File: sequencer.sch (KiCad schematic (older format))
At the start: 189 parts, among them IC1 ATMEGA328PB, IC2 AT24CS64-XHM, J13 SYNC IN, J14 TRIGGER OUT 1, J15 TRIGGER OUT 2, P3 CONN_02X02, P4 CONN_02X03, P5 CONN_02X03, P6 CONN_01X03, P7 CONN_01X04, Q38 MMBT3904, SW10 INST_CH_12, SW11 SHIFT, SW12 IF_VAR, SW13 INST_LT_4, SW14 INST_MT_5, SW15 INST_HT_6, SW16 INST_RS_7, SW17 INST_CP_8, SW18 INST_CB_9, SW19 INST_CY_10, SW2 BASIC_VAR_A, SW20 INST_OH_11, SW21 START/STOP, SW22 TAP, SW4 MODE, SW5 FILL, SW6 CLEAR, SW7 INST_AC_1, SW8 INST_BD_2, SW9 INST_SD_3, U27 74HC165, U28 74HC165, U29 74HC165, U30 74AC595, U31 74AC595, U32 74AC595, U33 74AC595, U34 74AC595, U35 R-78E5.0-1.0, U36 74AC595, U37 74AC595, X1 MIDI IN, Y1 16MHz

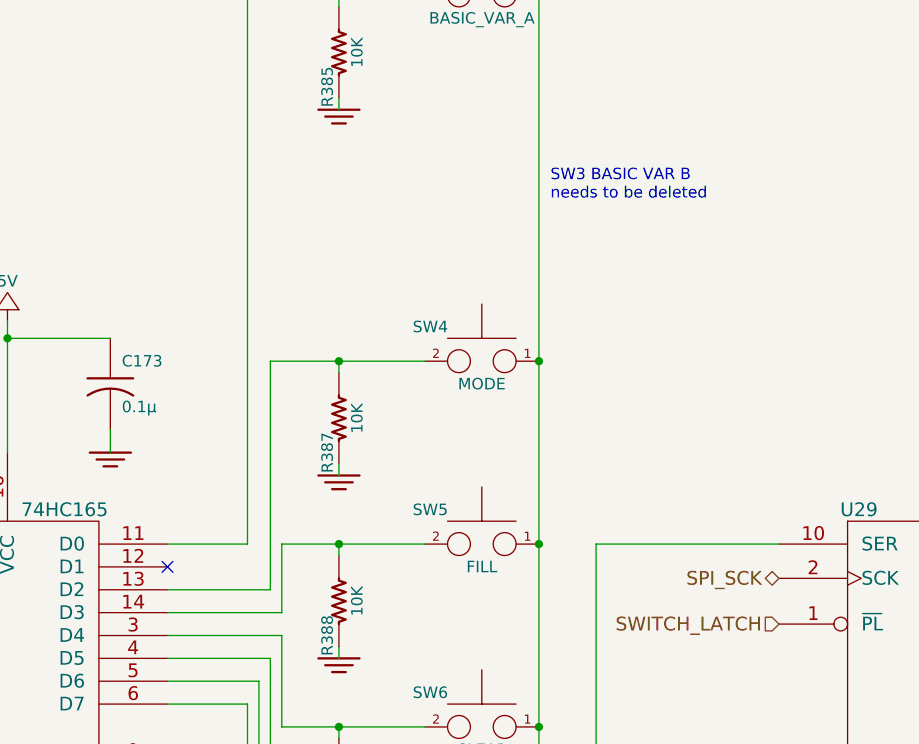
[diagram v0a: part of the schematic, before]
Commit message: made some notes on schematics. added beginnings of OM
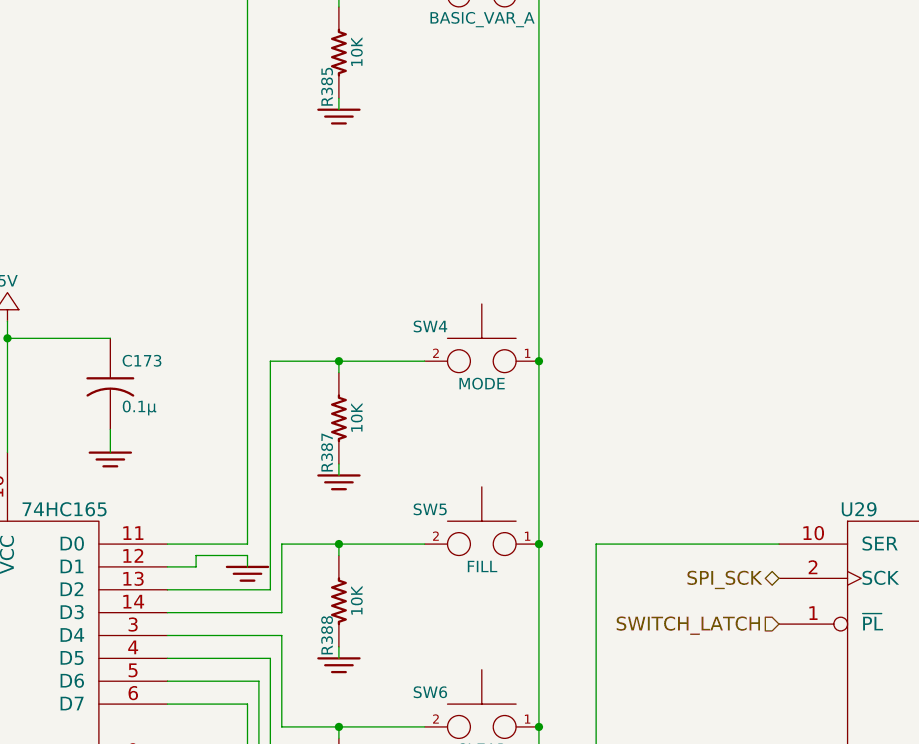
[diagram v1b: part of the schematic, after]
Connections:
- wire segments 592 -> 596
- no-connect marks 10 -> 9
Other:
- note removed: "SW3 BASIC VAR B \nneeds to be deleted"
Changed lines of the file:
@@
 Text GLabel 12700 3375 2    50   Input ~ 0
 SYNC_IN
-Text Notes 4325 6400 0    50   ~ 0
-SW3 BASIC VAR B \nneeds to be deleted
 Text GLabel 12700 2625 2    50   Output ~ 0
 SYNC_LED_R
@@
 Wire Wire Line
 	10675 10325 11100 10325
-NoConn ~ 2650 8000
 $Comp
 L GND_E #PWR0486
@@
 Wire Wire Line
 	7175 3825 7250 3825
+$Comp
+L GND_E #PWR?
+U 1 1 5893EC46
+P 3000 8000
+F 0 "#PWR?" V 3000 8000 30  0001 C CNN
+F 1 "GND_E" H 3000 7930 30  0001 C CNN
+F 2 "~" H 3000 8000 60  0000 C CNN
+F 3 "~" H 3000 8000 60  0000 C CNN
+	1    3000 8000
+	1    0    0    -1
+$EndComp
+Wire Wire Line
+	2650 8000 2775 8000
+Wire Wire Line
+	2775 8000 2775 7950
+Wire Wire Line
+	2775 7950 3000 7950
+Wire Wire Line
+	3000 7950 3000 8000
 $EndSCHEMATC

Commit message: added 47uF caps to 5V supplies for U37 and U37. required to reduce SPI noise
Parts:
- added C164, C166: 47μ, MyModules:jrl_c_elec_5x5.3, symbol CP_US
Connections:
- wire segments 596 -> 600
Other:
- note added: "BIG FAT DIGITAL RAIL\nFILTER CAP"
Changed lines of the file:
@@
 	7175 3825 7250 3825
 $Comp
-L GND_E #PWR?
+L GND_E #PWR0489
 U 1 1 5893EC46
 P 3000 8000
-F 0 "#PWR?" V 3000 8000 30  0001 C CNN
+F 0 "#PWR0489" V 3000 8000 30  0001 C CNN
 F 1 "GND_E" H 3000 7930 30  0001 C CNN
 F 2 "~" H 3000 8000 60  0000 C CNN
@@
 Wire Wire Line
 	3000 7950 3000 8000
+$Comp
+L CP_US C164
+U 1 1 58D6CD8E
+P 18050 6550
+F 0 "C164" H 18075 6650 50  0000 L CNN
+F 1 "47μ" H 18075 6425 50  0000 L CNN
+F 2 "MyModules:jrl_c_elec_5x5.3" H 18050 6550 60  0001 C CNN
+F 3 "" H 18050 6550 60  0000 C CNN
+	1    18050 6550
+	1    0    0    -1
+$EndComp
+$Comp
+L CP_US C166
+U 1 1 58D6CD95
+P 18050 10200
+F 0 "C166" H 18075 10300 50  0000 L CNN
+F 1 "47μ" H 18075 10075 50  0000 L CNN
+F 2 "MyModules:jrl_c_elec_5x5.3" H 18050 10200 60  0001 C CNN
+F 3 "" H 18050 10200 60  0000 C CNN
+	1    18050 10200
+	1    0    0    -1
+$EndComp
+Connection ~ 18050 10000
+Wire Wire Line
+	18050 10400 18050 10450
+Wire Wire Line
+	18050 10450 18300 10450
+Connection ~ 18300 10450
+Text Notes 18125 9950 1    60   ~ 0
+BIG FAT DIGITAL RAIL\nFILTER CAP
+Connection ~ 18050 6350
+Wire Wire Line
+	18050 6750 18050 6800
+Wire Wire Line
+	18050 6800 18300 6800
+Connection ~ 18300 6800
+Text Notes 18250 6300 1    60   ~ 0
+BIG FAT DIGITAL RAIL\nFILTER CAP
 $EndSCHEMATC

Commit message: all triggers consolidated into one connector
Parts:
- removed P3: CONN_02X02, MyModules:GH-TOP-4, symbol CONN_02X02
- removed P4, P5: CONN_02X03, MyModules:GH-TOP-6, symbol CONN_02X03
- added P3: CONN_02X10, Pin_Headers:Pin_Header_Straight_2x10_Pitch1.27mm_SMD, symbol CONN_02X10
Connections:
- net labels added: COMMON_TRIG
- wire segments 600 -> 604
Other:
- note added: "TRIGGER \nHEADER"
- note removed: "TRIGGER \nHEADERS"
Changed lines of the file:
@@
 	17850 6275 17850 6850
 Wire Wire Line
-	18300 6350 17850 6350
+	17850 6350 18300 6350
 Wire Wire Line
 	17850 8550 17850 8650
@@
 	17850 9950 17850 10500
 Wire Wire Line
-	18300 10000 17850 10000
+	17850 10000 18300 10000
 Wire Wire Line
 	17850 12200 17850 12300
@@
 Wire Wire Line
 	4600 3975 4750 3975
-$Comp
-L CONN_02X02 P3
-U 1 1 57DD315C
-P 11125 9325
-F 0 "P3" H 11125 9525 50  0000 C CNN
-F 1 "CONN_02X02" H 11125 9175 50  0000 C CNN
-F 2 "MyModules:GH-TOP-4" H 11125 8125 60  0001 C CNN
-F 3 "" H 11125 8125 60  0000 C CNN
-	1    11125 9325
-	1    0    0    -1
-$EndComp
-Text HLabel 9450 9225 0    50   Output ~ 0
+Text HLabel 11100 9000 0    50   Output ~ 0
 ACCENT
-Text HLabel 9950 9225 2    50   Output ~ 0
+Text HLabel 11100 9100 0    50   Output ~ 0
 BD_TRIG
-Text HLabel 9450 9325 0    50   Output ~ 0
+Text HLabel 11100 9300 0    50   Output ~ 0
 SD_TRIG
-Text HLabel 9950 9325 2    50   Output ~ 0
+Text HLabel 11100 9800 0    50   Output ~ 0
 LT_TRIG
-Text HLabel 9450 9425 0    50   Output ~ 0
+Text HLabel 11100 9700 0    50   Output ~ 0
 MT_TRIG
-Text HLabel 9950 9425 2    50   Output ~ 0
+Text HLabel 11100 9600 0    50   Output ~ 0
 HT_TRIG
-Text HLabel 10875 9275 0    50   Output ~ 0
+Text HLabel 11100 9500 0    50   Output ~ 0
 RS_TRIG
-Text HLabel 11375 9275 2    50   Output ~ 0
+Text HLabel 11100 9400 0    50   Output ~ 0
 CP_TRIG
 Text Notes 10950 8825 0    60   ~ 0
-TRIGGER \nHEADERS
+TRIGGER \nHEADER
 $Comp
 L GND_E #PWR0483
 U 1 1 57DD8A3A
-P 11475 9525
-F 0 "#PWR0483" V 11475 9525 30  0001 C CNN
-F 1 "GND_E" H 11475 9455 30  0001 C CNN
-F 2 "~" H 11475 9525 60  0000 C CNN
-F 3 "~" H 11475 9525 60  0000 C CNN
-	1    11475 9525
-	1    0    0    -1
-$EndComp
-Wire Wire Line
-	11375 9375 11475 9375
-Wire Wire Line
-	11475 9375 11475 9525
+P 12100 9550
+F 0 "#PWR0483" V 12100 9550 30  0001 C CNN
+F 1 "GND_E" H 12100 9480 30  0001 C CNN
+F 2 "~" H 12100 9550 60  0000 C CNN
+F 3 "~" H 12100 9550 60  0000 C CNN
+	1    12100 9550
+	1    0    0    -1
+$EndComp
 $Comp
 L 5V #PWR0484
 U 1 1 57DDA864
-P 10675 10050
-F 0 "#PWR0484" H 10675 9900 50  0001 C CNN
-F 1 "5V" H 10675 10225 50  0000 C CNN
-F 2 "" H 10675 10050 60  0000 C CNN
-F 3 "" H 10675 10050 60  0000 C CNN
-	1    10675 10050
-	1    0    0    -1
-$EndComp
-$Comp
-L CONN_02X03 P4
-U 1 1 57DDE11C
-P 11350 10225
-F 0 "P4" H 11350 10425 50  0000 C CNN
-F 1 "CONN_02X03" H 11350 10025 50  0000 C CNN
-F 2 "MyModules:GH-TOP-6" H 11350 9025 60  0001 C CNN
-F 3 "" H 11350 9025 60  0000 C CNN
-	1    11350 10225
-	1    0    0    -1
-$EndComp
-Text HLabel 10875 9375 0    50   Output ~ 0
+P 10300 8900
+F 0 "#PWR0484" H 10300 8750 50  0001 C CNN
+F 1 "5V" H 10300 9075 50  0000 C CNN
+F 2 "" H 10300 8900 60  0000 C CNN
+F 3 "" H 10300 8900 60  0000 C CNN
+	1    10300 8900
+	1    0    0    -1
+$EndComp
+Text HLabel 11100 9900 0    50   Output ~ 0
 MA_TRIG
-Text HLabel 11100 10125 0    50   Output ~ 0
+Text HLabel 11600 9700 2    50   Output ~ 0
 CB_TRIG
-Text HLabel 11600 10125 2    50   Output ~ 0
+Text HLabel 11600 9800 2    50   Output ~ 0
 CY_TRIG
-Text HLabel 11100 10225 0    50   Output ~ 0
+Text HLabel 11600 9900 2    50   Output ~ 0
 OH_TRIG
-Text HLabel 11600 10225 2    50   Output ~ 0
+Text HLabel 11600 9600 2    50   Output ~ 0
 CH_TRIG
 $Comp
 L GND_E #PWR0485
 U 1 1 57DE40B4
-P 11675 10500
-F 0 "#PWR0485" V 11675 10500 30  0001 C CNN
-F 1 "GND_E" H 11675 10430 30  0001 C CNN
-F 2 "~" H 11675 10500 60  0000 C CNN
-F 3 "~" H 11675 10500 60  0000 C CNN
-	1    11675 10500
-	1    0    0    -1
-$EndComp
-Wire Wire Line
-	11600 10325 11675 10325
-Wire Wire Line
-	11675 10325 11675 10500
-$Comp
-L CONN_02X03 P5
-U 1 1 57B54F0F
-P 9700 9325
-F 0 "P5" H 9700 9525 50  0000 C CNN
-F 1 "CONN_02X03" H 9700 9125 50  0000 C CNN
-F 2 "MyModules:GH-TOP-6" H 9700 8125 60  0001 C CNN
-F 3 "" H 9700 8125 60  0000 C CNN
-	1    9700 9325
-	1    0    0    -1
-$EndComp
-Wire Wire Line
-	10675 10050 10675 10325
-Wire Wire Line
-	10675 10325 11100 10325
+P 12450 7500
+F 0 "#PWR0485" V 12450 7500 30  0001 C CNN
+F 1 "GND_E" H 12450 7430 30  0001 C CNN
+F 2 "~" H 12450 7500 60  0000 C CNN
+F 3 "~" H 12450 7500 60  0000 C CNN
+	1    12450 7500
+	1    0    0    -1
+$EndComp
 $Comp
 L GND_E #PWR0486
@@
 Text Notes 18250 6300 1    60   ~ 0
 BIG FAT DIGITAL RAIL\nFILTER CAP
+$Comp
+L CONN_02X10 P3
+U 1 1 58DC7F14
+P 11350 9450
+F 0 "P3" H 11350 10000 50  0000 C CNN
+F 1 "CONN_02X10" V 11350 9450 50  0000 C CNN
+F 2 "Pin_Headers:Pin_Header_Straight_2x10_Pitch1.27mm_SMD" H 11350 8250 60  0000 C CNN
+F 3 "" H 11350 8250 60  0000 C CNN
+	1    11350 9450
+	1    0    0    -1
+$EndComp
+Text GLabel 11100 9200 0    60   Output ~ 0
+COMMON_TRIG
+$Comp
+L 5V #PWR0490
+U 1 1 58DF48F9
+P 11800 8900
+F 0 "#PWR0490" H 11800 8750 50  0001 C CNN
+F 1 "5V" H 11800 9075 50  0000 C CNN
+F 2 "" H 11800 8900 60  0000 C CNN
+F 3 "" H 11800 8900 60  0000 C CNN
+	1    11800 8900
+	1    0    0    -1
+$EndComp
+Wire Wire Line
+	10300 8900 10300 9000
+Wire Wire Line
+	10300 9000 10525 9000
+Wire Wire Line
+	11800 8900 11800 9100
+Wire Wire Line
+	11800 9000 11600 9000
+Wire Wire Line
+	11800 9100 11600 9100
+Connection ~ 11800 9000
+Wire Wire Line
+	11600 9200 12100 9200
+Wire Wire Line
+	12100 9200 12100 9550
+Wire Wire Line
+	11600 9300 12100 9300
+Connection ~ 12100 9300
+Wire Wire Line
+	11600 9400 12100 9400
+Connection ~ 12100 9400
+Wire Wire Line
+	11600 9500 12100 9500
+Connection ~ 12100 9500
 $EndSCHEMATC

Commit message: added 5V to 12V selectable trigger output for TRIG OUT 2
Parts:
- removed P7: CONN_01X04, MyModules:GH-TOP-4, symbol CONN_01X04
- removed Q38: MMBT3904, MyModules:SOT23-132-JRL, symbol MMBT3904
- added P12: CONN_01X03, Pin_Headers:Pin_Header_Straight_1x03_Pitch2.54mm, symbol CONN_01X03
- added P7: CONN_02X03, DIY:PIN_ARRAY_3X2, symbol CONN_02X03
- added Q38, Q64: C945, MyModules:SOT23-132-JRL, symbol C945
- added Q75: A733, MyModules:SOT23-132-JRL, symbol A733
- added R393, R457: 22K, MyModules:SM0603-R-JRL, symbol R_US
- added R456, R458: 10K, MyModules:SM0603-R-JRL, symbol R_US
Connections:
- net DIN_FILL: now also P7.2 (P2)
- net DIN_RESET: now also P7.1 (P1)
- net DIN_RUN_STOP: now also P7.4 (P4)
- net DIN_TEMPO_CLK: now also P7.6 (P6)
- net GND: now also P7.3 (P3), Q38.2 (E), Q64.2 (E), R456.1
- net SYNC_IN: now also Q38.3 (C)
- net TRIG_OUT_2: now also P12.3 (P3), R393.2; no longer J15.3
- net UART_TX: now also P7.5 (P5)
- net V+: now also Q75.3 (C), R458.2
- net at R380.2, R451.1: now also Q38.1 (B)
- new net: J15.3, P12.2 (P2)
- new net: Q64.1 (B), R393.1, R456.2
- new net: Q64.3 (C), R457.2
- new net: Q75.1 (B), R457.1, R458.1
- new net TRIG_OUT_12V: P12.1 (P1), Q75.2 (E)

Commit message: few tweaks, ready to generate gerbers for 2.1 production prototype
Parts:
- added P13, P14: CONN_01X01, MyModules:TEST_POINT_SMALL, symbol CONN_01X01
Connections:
- net +5V: now also P13.1 (P1)
- net GND: now also P14.1 (P1)

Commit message: added input protection fuses, fixed trigger level converter, few tweaks
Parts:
- added R459: 10K, MyModules:SM0603-R-JRL, symbol R_US
- R457: value 22K -> 10K
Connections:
- net GND: now also R459.1
- net TRIG_OUT_12V: now also Q75.3 (C), R459.2; no longer Q75.2 (E)
- net V+: now also Q75.2 (E); no longer Q75.3 (C)
- net at Q64.3 (C), R457.2: now also R458.1
- net at Q75.1 (B), R457.1: no longer R458.1
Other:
- note added: "CAT24C512\n"
- note added: "Need to add protection/\nrectification here?\n"
- moved on the sheet: R458
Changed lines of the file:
@@
 F 3 "" H 15200 4525 50  0000 L CNN
 	1    15200 4525
-	1    0    0    -1
+	1    0    0    1
 $EndComp
 Wire Wire Line
@@
 	14425 5025 14425 5350
 Wire Wire Line
-	14425 5350 14050 5350
+	14050 5350 15300 5350
 Wire Wire Line
 	14050 5300 14050 5425
@@
 L R_US R458
 U 1 1 5903EC77
-P 14975 4250
-F 0 "R458" H 15125 4200 50  0000 C CNN
-F 1 "10K" H 15100 4275 50  0000 C CNN
-F 2 "MyModules:SM0603-R-JRL" H 14975 4250 60  0001 C CNN
-F 3 "~" H 14975 4250 60  0000 C CNN
-	1    14975 4250
+P 14525 4250
+F 0 "R458" H 14675 4200 50  0000 C CNN
+F 1 "10K" H 14650 4275 50  0000 C CNN
+F 2 "MyModules:SM0603-R-JRL" H 14525 4250 60  0001 C CNN
+F 3 "~" H 14525 4250 60  0000 C CNN
+	1    14525 4250
 	-1   0    0    1
 $EndComp
@@
 P 14750 4525
 F 0 "R457" V 14650 4525 50  0000 C CNN
-F 1 "22K" V 14850 4525 50  0000 C CNN
+F 1 "10K" V 14850 4525 50  0000 C CNN
 F 2 "MyModules:SM0603-R-JRL" H 14750 4525 60  0001 C CNN
 F 3 "~" H 14750 4525 60  0000 C CNN
@@
 	14425 4525 14425 4625
 Wire Wire Line
-	14975 4450 14975 4525
+	14950 4525 15000 4525
 Wire Wire Line
-	14950 4525 15000 4525
-Connection ~ 14975 4525
-Wire Wire Line
-	14975 4050 14975 3975
-Wire Wire Line
-	14975 3975 15300 3975
+	14525 3975 15300 3975
 Connection ~ 15300 3975
 Text GLabel 10800 5050 2    50   Input ~ 0
 TRIG_OUT_12V
-Text GLabel 15375 4925 2    50   Output ~ 0
+Text GLabel 15400 4875 2    50   Output ~ 0
 TRIG_OUT_12V
 Wire Wire Line
 	15300 4725 15300 4925
-Wire Wire Line
-	15300 4925 15375 4925
 Text HLabel 15300 3850 1    60   Input ~ 0
 V+
@@
 	0    -1   -1   0
 $EndComp
+Text Notes 15225 3325 0    50   ~ 0
+CAT24C512\n
+Text Notes 950  3825 0    50   ~ 0
+Need to add protection/\nrectification here?\n
+Wire Wire Line
+	14525 3975 14525 4050
+Wire Wire Line
+	14525 4450 14525 4525
+Connection ~ 14525 4525
+$Comp
+L R_US R459
+U 1 1 59E53E24
+P 15300 5125
+F 0 "R459" H 15450 5075 50  0000 C CNN
+F 1 "10K" H 15425 5150 50  0000 C CNN
+F 2 "MyModules:SM0603-R-JRL" H 15300 5125 60  0001 C CNN
+F 3 "~" H 15300 5125 60  0000 C CNN
+	1    15300 5125
+	-1   0    0    1
+$EndComp
+Wire Wire Line
+	15300 5350 15300 5325
+Connection ~ 14425 5350
+Wire Wire Line
+	15400 4875 15300 4875
+Connection ~ 15300 4875
 $EndSCHEMATC

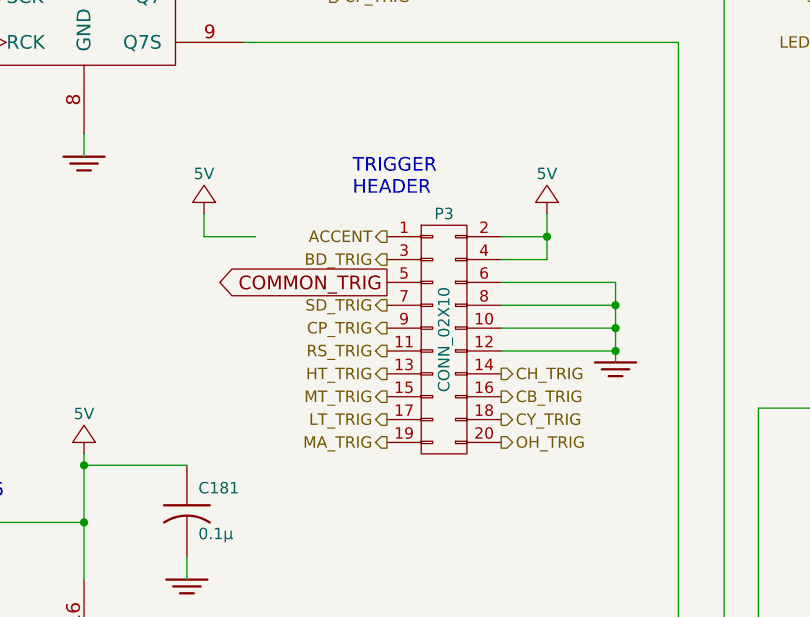
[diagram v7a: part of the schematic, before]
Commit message: changed P3 trigger expander connector, added TRIG signal to expander connector, twiddled and diddled traces and ground plane
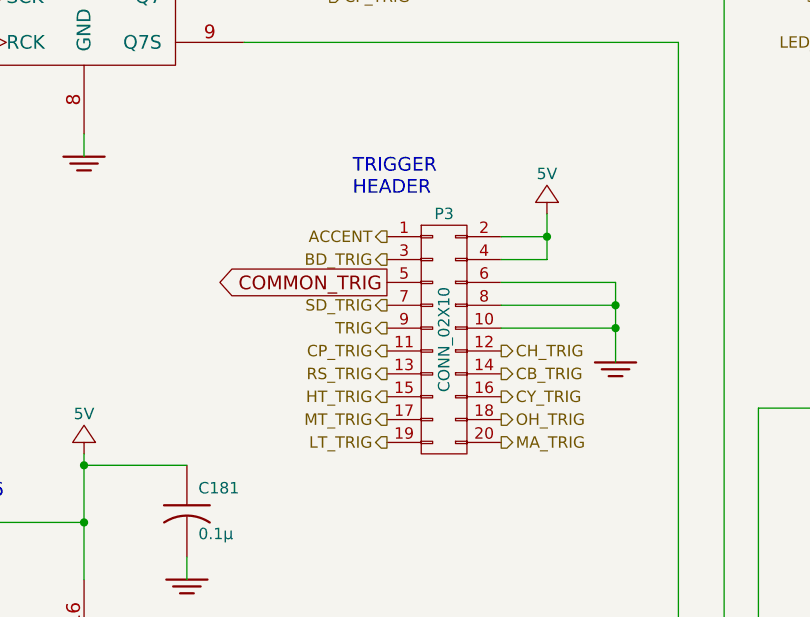
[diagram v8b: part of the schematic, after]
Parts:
- P3: footprint Pin_Headers:Pin_Header_Straight_2x10_Pitch1.27mm_SMD -> Pin_Headers:Pin_Header_Straight_2x10_Pitch2.54mm
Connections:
- net CB_TRIG: now also P3.14 (P14); no longer P3.16 (P16)
- net CH_TRIG: now also P3.12 (P12); no longer P3.14 (P14)
- net CP_TRIG: now also P3.11 (P11); no longer P3.9 (P9)
- net CY_TRIG: now also P3.16 (P16); no longer P3.18 (P18)
- net GND: no longer P3.12 (P12)
- net HT_TRIG: now also P3.15 (P15); no longer P3.13 (P13)
- net LT_TRIG: now also P3.19 (P19); no longer P3.17 (P17)
- net MA_TRIG: now also P3.20 (P20); no longer P3.19 (P19)
- net MT_TRIG: now also P3.17 (P17); no longer P3.15 (P15)
- net OH_TRIG: now also P3.18 (P18); no longer P3.20 (P20)
- net RS_TRIG: now also P3.13 (P13); no longer P3.11 (P11)
- net TRIG: now also P3.9 (P9)
